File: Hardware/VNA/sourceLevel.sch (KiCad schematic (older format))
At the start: 26 parts, among them U7 AD8319, U8 SKY12347-362LF, U9 TRF37A75

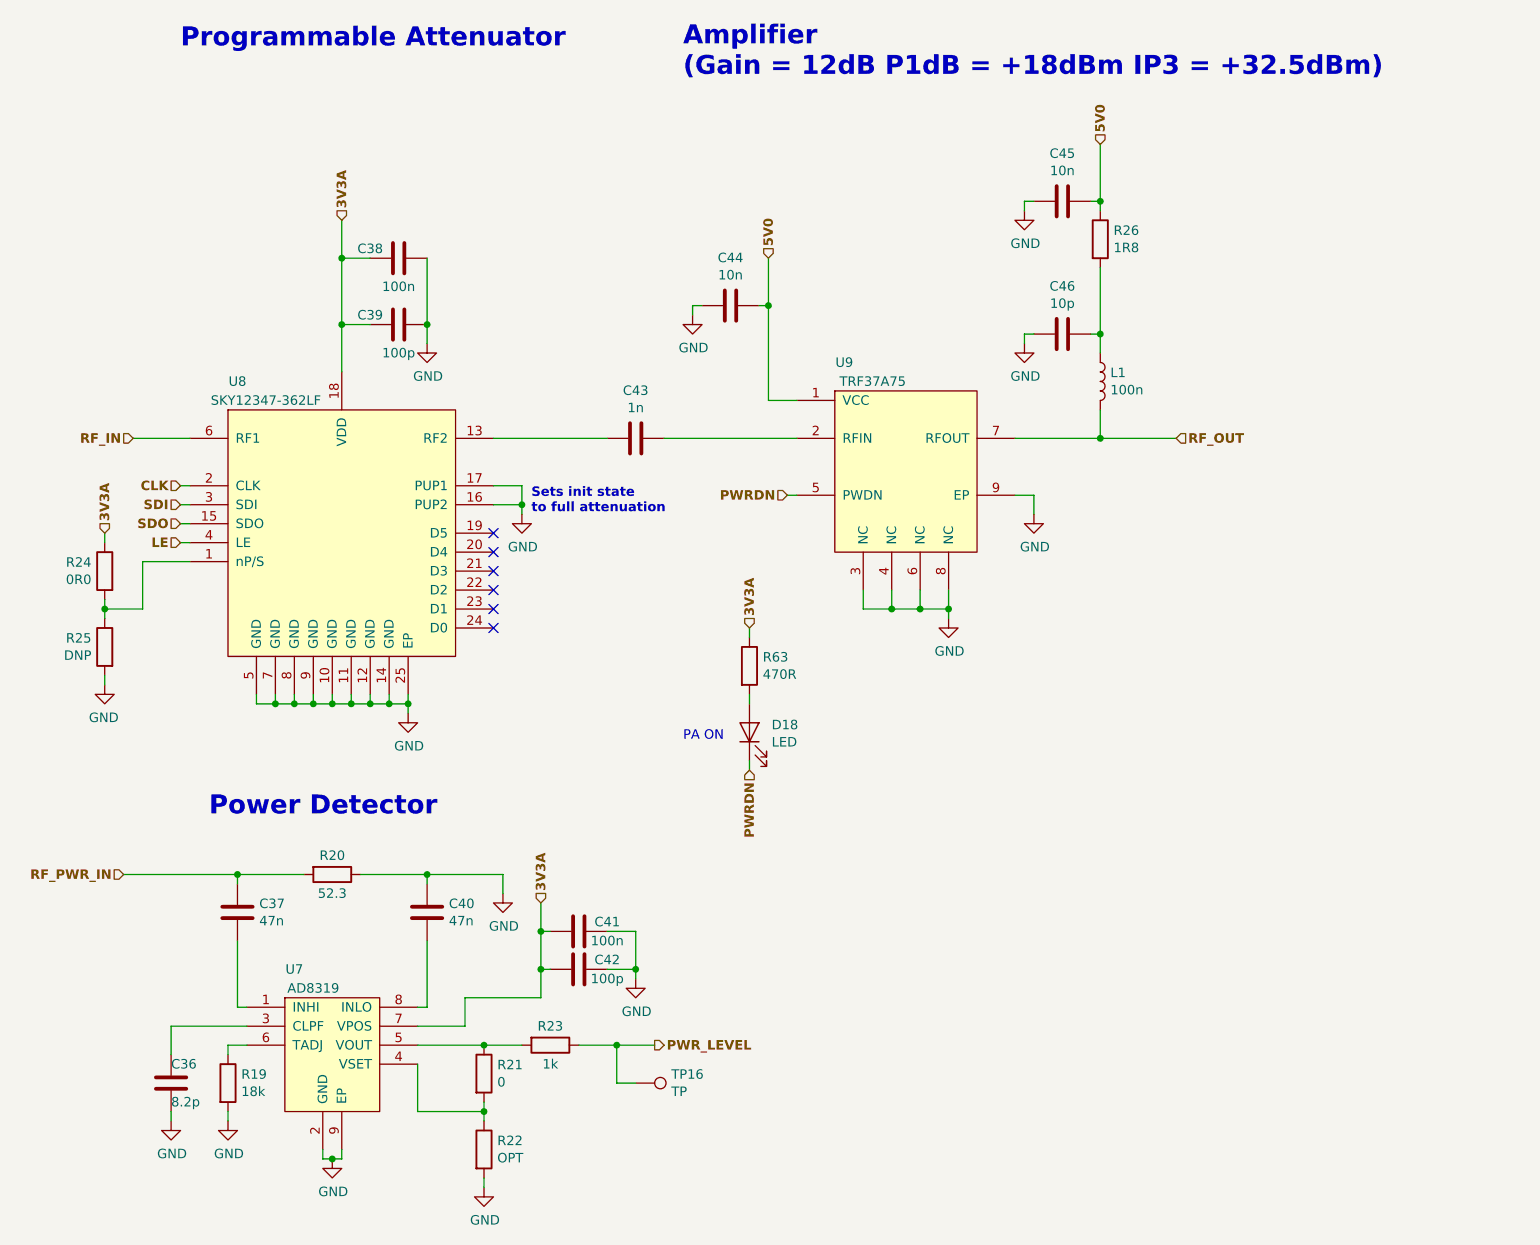
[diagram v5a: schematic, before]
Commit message: fix KiCad 5.1.0 bold after plot issue on schematics
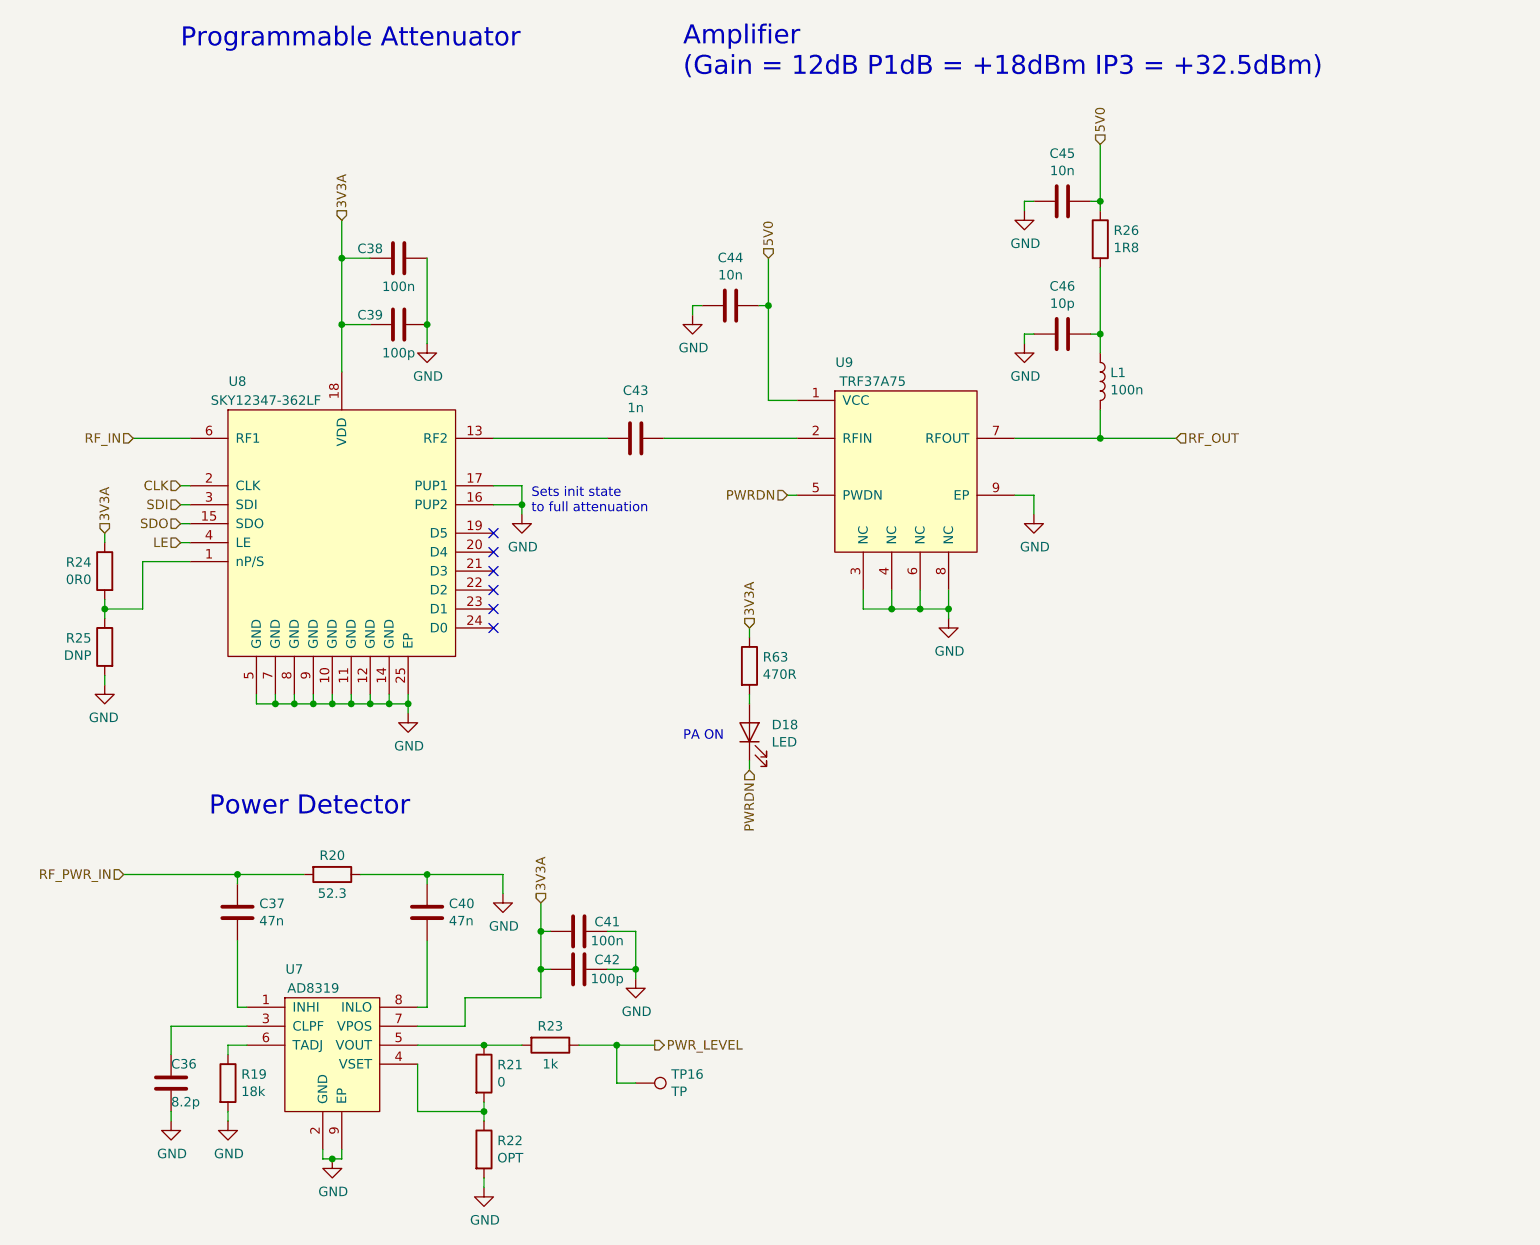
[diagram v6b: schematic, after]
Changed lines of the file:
@@
 	4050 1950 4050 2300
 Connection ~ 4050 2300
-Text Notes 2750 850  0    100  ~ 20
+Text Notes 2750 850  0    100  ~ 0
 Programmable Attenuator
 Wire Wire Line
@@
 Wire Wire Line
 	4400 2900 5000 2900
-Text HLabel 2500 2900 0    50   Input ~ 10
+Text HLabel 2500 2900 0    50   Input ~ 0
 RF_IN
 Wire Wire Line
@@
 Wire Wire Line
 	4850 6100 5050 6100
-Text Notes 2900 4900 0    100  ~ 20
+Text Notes 2900 4900 0    100  ~ 0
 Power Detector\n
 $Comp
@@
 Wire Wire Line
 	5150 5700 5150 5750
-Text HLabel 2450 5200 0    50   Input ~ 10
+Text HLabel 2450 5200 0    50   Input ~ 0
 RF_PWR_IN
-Text HLabel 5250 6100 2    50   Output ~ 10
+Text HLabel 5250 6100 2    50   Output ~ 0
 PWR_LEVEL
-Text HLabel 3600 1750 1    50   Input ~ 10
+Text HLabel 3600 1750 1    50   Input ~ 0
 3V3A
-Text HLabel 4650 5350 1    50   Input ~ 10
+Text HLabel 4650 5350 1    50   Input ~ 0
 3V3A
 $Comp
@@
 Wire Wire Line
 	2350 3800 2350 3850
-Text HLabel 2750 3250 0    50   Input ~ 10
+Text HLabel 2750 3250 0    50   Input ~ 0
 SDI
-Text HLabel 2750 3150 0    50   Input ~ 10
+Text HLabel 2750 3150 0    50   Input ~ 0
 CLK
-Text HLabel 2750 3450 0    50   Input ~ 10
+Text HLabel 2750 3450 0    50   Input ~ 0
 LE
-Text HLabel 2350 3400 1    50   Input ~ 10
+Text HLabel 2350 3400 1    50   Input ~ 0
 3V3A
 Wire Wire Line
@@
 Wire Wire Line
 	2800 3350 2750 3350
-Text HLabel 2750 3350 0    50   Input ~ 10
+Text HLabel 2750 3350 0    50   Input ~ 0
 SDO
 Wire Wire Line
@@
 	1    0    0    -1
 $EndComp
-Text Notes 4600 3300 0    50   ~ 10
+Text Notes 4600 3300 0    50   ~ 0
 Sets init state \nto full attenuation
 Wire Wire Line
@@
 Wire Wire Line
 	7200 1650 7200 1700
-Text HLabel 5950 3200 0    50   Input ~ 10
+Text HLabel 5950 3200 0    50   Input ~ 0
 PWRDN
 Wire Wire Line
@@
 Wire Wire Line
 	6800 3800 6800 3700
-Text HLabel 7600 1350 1    50   Input ~ 10
+Text HLabel 7600 1350 1    50   Input ~ 0
 5V0
-Text HLabel 5850 1950 1    50   Input ~ 10
+Text HLabel 5850 1950 1    50   Input ~ 0
 5V0
 Wire Wire Line
@@
 Wire Wire Line
 	7600 1650 7600 1700
-Text Notes 5400 1000 0    100  ~ 20
+Text Notes 5400 1000 0    100  ~ 0
 Amplifier \n(Gain = 12dB P1dB = +18dBm IP3 = +32.5dBm)
-Text HLabel 8000 2900 2    50   Input ~ 10
+Text HLabel 8000 2900 2    50   Input ~ 0
 RF_OUT
 Wire Wire Line
@@
 	1    0    0    -1
 $EndComp
-Text HLabel 5750 4650 3    50   Input ~ 10
+Text HLabel 5750 4650 3    50   Input ~ 0
 PWRDN
 Wire Wire Line
@@
 Wire Wire Line
 	5750 4600 5750 4650
-Text HLabel 5750 3900 1    50   Input ~ 10
+Text HLabel 5750 3900 1    50   Input ~ 0
 3V3A
 Wire Wire Line
